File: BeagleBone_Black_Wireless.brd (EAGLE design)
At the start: 86.4 x 54.6 mm, 274 parts, among them IC1 OSD3358, IC10 TXS0108ERGYR, IC11 TXS0108ERGYR, IC12 TPS2051BDGN, IC13 SN74AUC1G74, IC14 TPD4S012DRY, IC15 TPD4S012DRY, IC17 SN74LVC2G241DCUR, IC18 TL1963ADCQR, IC19 AP2112K-1.8TRG1 3.3V, IC2 SN74LVC1G07DCK, IC3 SN74LVC1G06DCK, IC4 24LC32AT-I/OT, IC5 TLVH431 (SOT-23-3), IC6 DNP TLVH431 (SOT-23-3), IC7 IP4283CZ10-TBR, IC8 IP4283CZ10-TBR, Q2 32.768kHz, Q4 24 MHz, T1 MMBT2907, T2 DNP MMBT2907, T3 BSS138W-7-F, T4 BSS138W-7-F, X2 SCHA5B0200, X4 10118192-0001LF, X5 10118241-001RLF

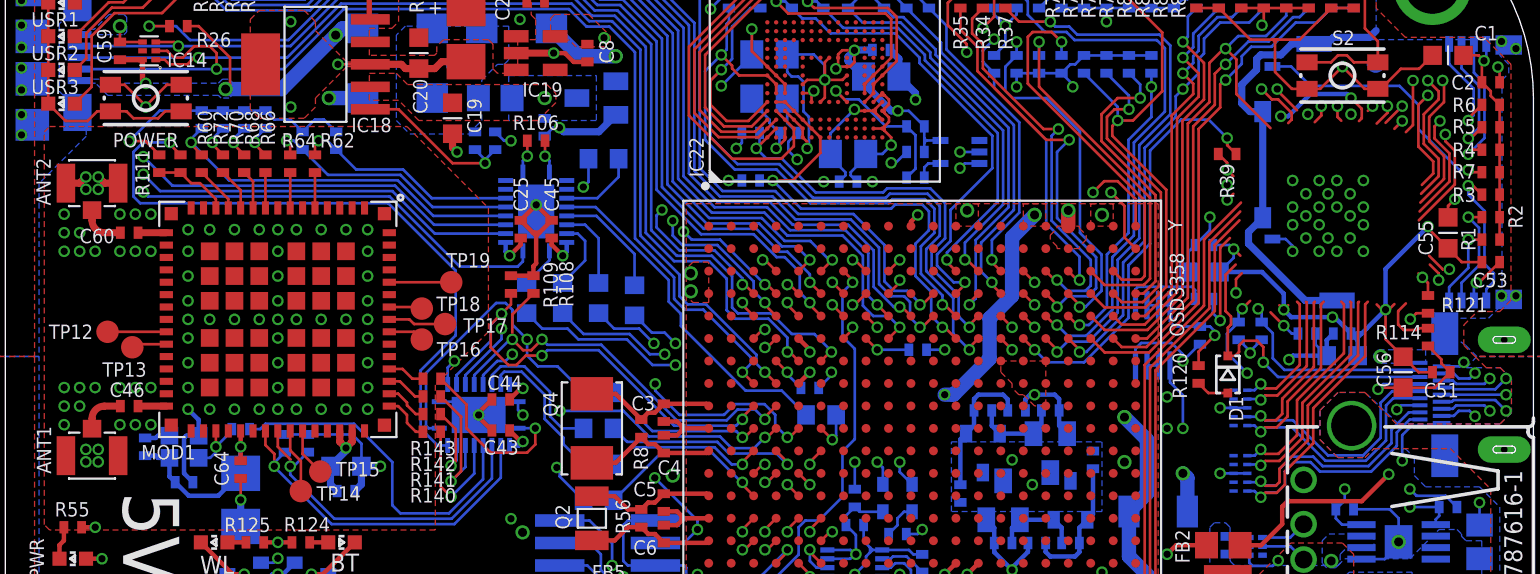
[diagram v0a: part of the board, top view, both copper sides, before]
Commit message: removed MOD1 - added IC9 - adjusted routes
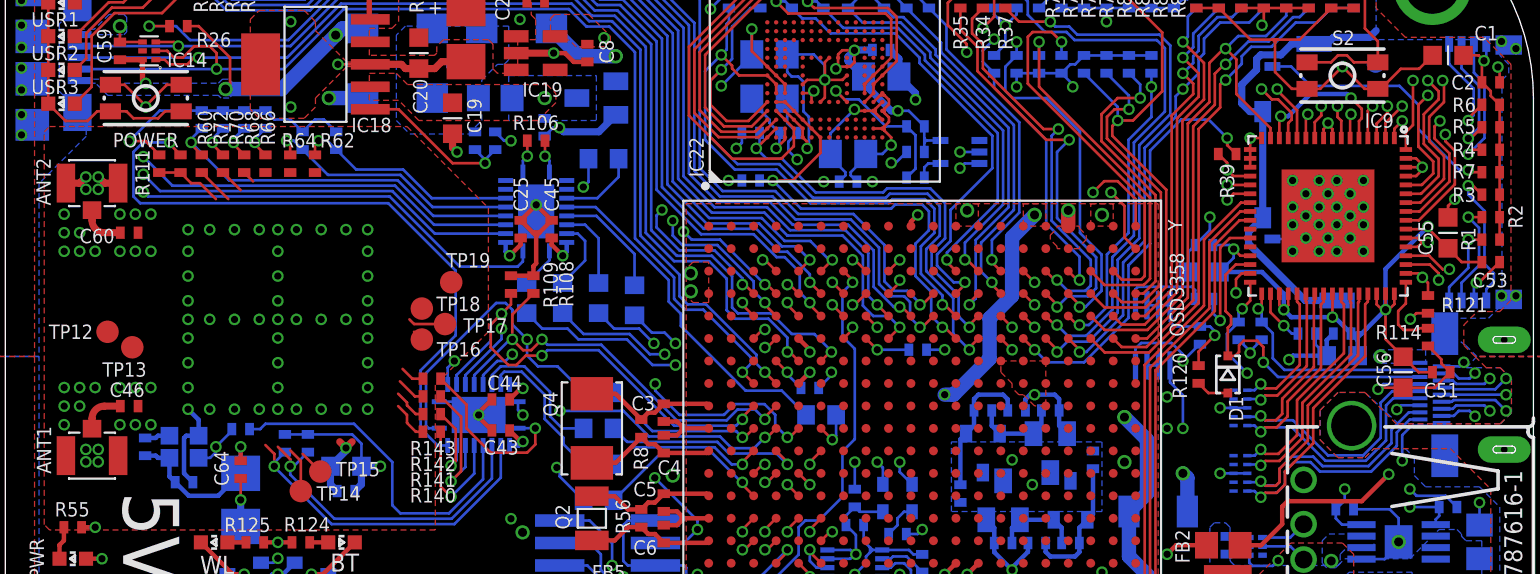
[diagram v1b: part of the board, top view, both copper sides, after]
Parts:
- removed MOD1: WL1835MODGBMOCT, GHI-IC:MOC-100(TI)
- added IC9: TDA19988BHN/C1,557, GHI-IC:SOT804-4(NXP)
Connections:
- net 1.8V-WIFI: no longer MOD1.38
- net 12MHZ: now also IC9.27
- net 3.3V-WIFI: no longer MOD1.46, MOD1.47
- net 32.768KHZ: no longer MOD1.36
- net BT_EN: no longer MOD1.41
- net CEC: now also IC9.30
- net EXT_SWING: now also IC9.34
- net GND: now also IC9.16, IC9.17, IC9.18, IC9.19, IC9.53, IC9.54, IC9.61, IC9.62, IC9.63, IC9.65, IC9.8, IC9.9; no longer MOD1.1, MOD1.15, MOD1.16, MOD1.17, MOD1.19, MOD1.20, MOD1.23, MOD1.24, MOD1.28, MOD1.29, MOD1.30, MOD1.31, MOD1.33, MOD1.34, MOD1.35, MOD1.37, MOD1.39, MOD1.44, MOD1.45, MOD1.48, MOD1.49, MOD1.54, MOD1.55, MOD1.59, MOD1.61, MOD1.63, MOD1.64, MOD1.7, MOD1.9, MOD1.G1, MOD1.G10, MOD1.G11, MOD1.G12, MOD1.G13, MOD1.G14, MOD1.G15, MOD1.G16, MOD1.G17, MOD1.G18, MOD1.G19, MOD1.G2, MOD1.G20, MOD1.G21, MOD1.G22, MOD1.G23, MOD1.G24, MOD1.G25, MOD1.G26, MOD1.G27, MOD1.G28, MOD1.G29, MOD1.G3, MOD1.G30, MOD1.G31, MOD1.G32, MOD1.G33, MOD1.G34, MOD1.G35, MOD1.G36, MOD1.G4, MOD1.G5, MOD1.G6, MOD1.G7, MOD1.G8, MOD1.G9
- net HDMI.DSCL: now also IC9.33
- net HDMI.DSDA: now also IC9.32
- net HDMI_1V8: now also IC9.14, IC9.29, IC9.35, IC9.36, IC9.41, IC9.46, IC9.47, IC9.48, IC9.5, IC9.55
- net HDMI_INT: now also IC9.50
- net HPD: now also IC9.31
- net I2C0_SCL: now also IC9.52
- net I2C0_SDA: now also IC9.51
- net LCD.CLOCK: now also IC9.4
- net LCD.D0.B0--B3: now also IC9.15
- net LCD.D1.B1--B4: now also IC9.13
- net LCD.D10.G5--G7: now also IC9.64
- net LCD.D11.R0--R3: now also IC9.60
- net LCD.D12.R1--R4: now also IC9.59
- net LCD.D13.R2--R5: now also IC9.58
- net LCD.D14.R3--R6: now also IC9.57
- net LCD.D15.R4--R7: now also IC9.56
- net LCD.D2.B2--B5: now also IC9.12
- net LCD.D3.B3--B6: now also IC9.11
- net LCD.D4.B4--B7: now also IC9.10
- net LCD.D5.G0--G2: now also IC9.7
- net LCD.D6.G1--G3: now also IC9.6
- net LCD.D7.G2--G4: now also IC9.3
- net LCD.D8.G3--G5: now also IC9.2
- net LCD.D9.G4--G6: now also IC9.1
- net LCD.ENABLE: now also IC9.20
- net LCD.HSYNC: now also IC9.22
- net LCD.VSYNC: now also IC9.21
- net N$15: no longer MOD1.32
- net N$19: no longer MOD1.18
- net N$33: no longer MOD1.26
- net N$35: no longer MOD1.27
- net N$38: no longer MOD1.42
- net N$39: no longer MOD1.43
- net N$40: no longer MOD1.56
- net N$41: no longer MOD1.57
- net N$43: no longer MOD1.58
- net N$44: no longer MOD1.60
- net N$62: no longer MOD1.14
- net N$63: no longer MOD1.13
- net N$64: no longer MOD1.12
- net N$65: no longer MOD1.11
- net N$67: no longer MOD1.10
- net N$69: no longer MOD1.8
- net N$70: no longer MOD1.6
- net N$93: no longer MOD1.50
- net N$94: no longer MOD1.51
- net N$95: no longer MOD1.52
- net N$96: no longer MOD1.53
- net SPI1_CS0: now also IC9.25
- net SPI1_D0: now also IC9.24
- net SPI1_SCLK: now also IC9.23
- net TEST: now also IC9.49
- net TX0+: now also IC9.40
- net TX0-: now also IC9.39
- net TX1+: now also IC9.43
- net TX1-: now also IC9.42
- net TX2+: now also IC9.45
- net TX2-: now also IC9.44
- net TXC+: now also IC9.38
- net TXC-: now also IC9.37
- net WL_EN: no longer MOD1.40
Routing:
- net GND: track 301.1 -> 311.6 mm, vias 154 -> 159
- net HDMI_1V8: track 72.2 -> 80.7 mm
- net N$44: track 3.50 -> 0.00 mm
- net N$33: track 3.32 -> 0.00 mm
- net VIN_BAT: track 71.6 -> 69.1 mm
- net N$70: track 2.00 -> 0.00 mm
- net N$69: track 2.00 -> 0.00 mm
- net N$67: track 2.00 -> 0.00 mm
- net N$43: track 1.87 -> 0.12 mm
- net N$35: track 2.00 -> 0.25 mm
- net N$19: track 1.60 -> 0.00 mm
- net N$15: track 1.60 -> 0.00 mm
- net LCD.D2.B2--B5: track 47.3 -> 48.9 mm
- net LCD.CLOCK: track 47.0 -> 48.5 mm
- net N$65: track 2.21 -> 0.71 mm
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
